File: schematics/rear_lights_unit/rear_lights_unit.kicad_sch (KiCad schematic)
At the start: 0 parts

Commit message: schematic updates for bike computer, rear light unit, rear light unit control box
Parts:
- added BT1: Battery_Cell, symbol Device:Battery_Cell
- added C1, C3: 10nF, symbol Device:C
- added C2, C4: 10uF, symbol Device:C
- added D1, D10, D11, D12, D13, D14, D15, D16, D17, D18, D19, D2, D20, D21, D22, D23, D24, D3, D4, D5, D6, D7, D8, D9: LED, symbol Device:LED
- added J1: Conn_01x04_Socket, symbol Connector:Conn_01x04_Socket
- added Q1, Q2: IRLZ44N, Package_TO_SOT_THT:TO-220-3_Vertical, symbol Transistor_FET:IRLZ44N
- added R1, R10, R11, R12, R13, R14, R15, R16, R17, R18, R19, R2, R20, R21, R22, R23, R24, R3, R4, R5, R6, R7, R8, R9: 120, symbol Device:R
- added R25, R29: 7.5k, symbol Device:R
- added R26, R30: 75k, symbol Device:R
- added R27, R32: 100, symbol Device:R
- added R28, R31: 10k, symbol Device:R
- added U1, U2: LMC555xN, Package_DIP:DIP-8_W7.62mm, symbol Timer:LMC555xN
- added U3: TP4056 module, ..., symbol FarrhadTech:TP4056
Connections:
- new net: D1.1 (K), D2.1 (K), D3.1 (K), D4.1 (K), D5.1 (K), D6.1 (K), D7.1 (K), D8.1 (K), Q1.2 (D)
- new net: D4.2 (A), R4.1
- new net: D7.2 (A), R7.1
- new net: D12.2 (A), R12.1
- new net: D16.2 (A), R16.1
- new net: D10.1 (K), D11.1 (K), D12.1 (K), D13.1 (K), D14.1 (K), D15.1 (K), D16.1 (K), D9.1 (K), Q2.2 (D)
- new net: D11.2 (A), R11.1
- new net: D20.2 (A), R20.1
- new net: D21.2 (A), R21.1
- new net: D1.2 (A), R1.1
- new net: R27.1, U1.3 (Q)
- new net: Q1.1 (G), R27.2, R28.2
- new net: BT1.1 (+), U3.3 (B+)
- new net: BT1.2 (-), U3.4 (B-)
- new net: C4.2, R30.1, U2.2 (TR), U2.6 (THR)
- new net: R29.1, R30.2, U2.7 (DIS)
- new net: D23.2 (A), R23.1
- new net: D8.2 (A), R8.1
- new net: D18.2 (A), R18.1
- new net: D6.2 (A), R6.1
- new net: D5.2 (A), R5.1
- new net: D24.2 (A), R24.1
- new net: D14.2 (A), R14.1
- new net: D10.2 (A), R10.1
- new net: Q2.1 (G), R31.2, R32.2
- new net: D9.2 (A), R9.1
- new net: R25.1, R26.2, U1.7 (DIS)
- new net: C2.2, R26.1, U1.2 (TR), U1.6 (THR)
- new net: D3.2 (A), R3.1
- new net: D2.2 (A), R2.1
- new net: D15.2 (A), R15.1
- new net: C1.1, U1.5 (CV)
- new net: D13.2 (A), R13.1
- new net: D19.2 (A), R19.1
- new net: R32.1, U2.3 (Q)
- new net: D22.2 (A), R22.1
- new net: D17.2 (A), R17.1
- new net: C3.1, U2.5 (CV)
- new net GND: C1.2, C2.1, C3.2, C4.1, D17.1 (K), D18.1 (K), D19.1 (K), D20.1 (K), D21.1 (K), D22.1 (K), D23.1 (K), D24.1 (K), J1.4 (Pin_4), Q1.3 (S), Q2.3 (S), R28.1, R31.1, U1.1 (GND), U2.1 (GND), U3.5 (OUT-)
- new net LEFT_TURN_EN: J1.2 (Pin_2), R25.2, U1.4 (R)
- new net RIGHT_TURN_EN: J1.1 (Pin_1), R29.2, U2.4 (R)
- new net V+: J1.3 (Pin_3), R1.2, R10.2, R11.2, R12.2, R13.2, R14.2, R15.2, R16.2, R17.2, R18.2, R19.2, R2.2, R20.2, R21.2, R22.2, R23.2, R24.2, R3.2, R4.2, R5.2, R6.2, R7.2, R8.2, R9.2, U1.8 (VCC), U2.8 (VCC), U3.5 (OUT-)
- no-connect marks 0 -> 2
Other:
- note added: "D"
- note added: "G"
- note added: "JST connector (right angle)"
- note added: "LEFT TURN SIGNAL: yellow LEDs, flash when on"
- note added: "NOTES All LEDs used are CHANZON brand, 5 mm packages. Each has a forward voltage of 2 V and a forward current of 20 mA. To calculate the current limiting resistor value at maximum battery voltage: V = IR ->(4.2 V - 2 V) = (20 mA)R -> R = 110 ohms To allow for resistor tolerances, I rounded up to the next standard value of 120 ohms. To calculate the current through the LEDs at minimum battery volt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"
- note added: "REAR LIGHT: red LEDs, always on"
- note added: "RIGHT TURN SIGNAL: yellow LEDs, flash when on"
- note added: "S"
- note added: "Samsung 30Q 18650 (3000 mAH, 3.7 V nominal)"

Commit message: more schematic updates
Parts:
- added SW1: rocker_switch, symbol Switch:SW_SPST
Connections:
- net V+: now also SW1.2 (B); no longer U3.5 (OUT-)
- new net: SW1.1 (A), U3.5 (OUT-)
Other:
- note added: "NOTES All LEDs used are CHANZON brand, 5 mm packages. Each has a forward voltage of 2 V and a forward current of 20 mA. To calculate the current limiting resistor value at maximum battery voltage: V = IR =(4.2 V - 2 V) = (20 mA)R -> R = 110 ohms. To account for resistor tolerances, I rounded up to the next standard value of 120 ohms. Calculating the current through the LEDs at minimum battery vol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"
- note added: "This switch connects the rest of the system to the battery for power. Make sure it is turned to the "off" position when charging the battery to ensure correct operation!"
- note added: "right angle JST"
- note removed: "JST connector (right angle)"
- note removed: "NOTES All LEDs used are CHANZON brand, 5 mm packages. Each has a forward voltage of 2 V and a forward current of 20 mA. To calculate the current limiting resistor value at maximum battery voltage: V = IR ->(4.2 V - 2 V) = (20 mA)R -> R = 110 ohms To allow for resistor tolerances, I rounded up to the next standard value of 120 ohms. To calculate the current through the LEDs at minimum battery volt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"
- moved on the sheet: BT1, C1, C2, C3, C4, D1, D10, D11, D12, D13, D14, D15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

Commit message: finalized rear light unit schematic, added corresponding BOM
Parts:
- removed SW1: rocker_switch, symbol Switch:SW_SPST
- added C5: 10uF, symbol Device:C
- added SW2: rocker_switch, symbol Switch:SW_SPST
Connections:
- net GND: now also C5.2
- net V+: now also C5.1, SW2.2 (B)
- new net: SW2.1 (A), U3.5 (OUT-)
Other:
- note added: "This connector breaks out the signals to/from the control box (on handlebars)"

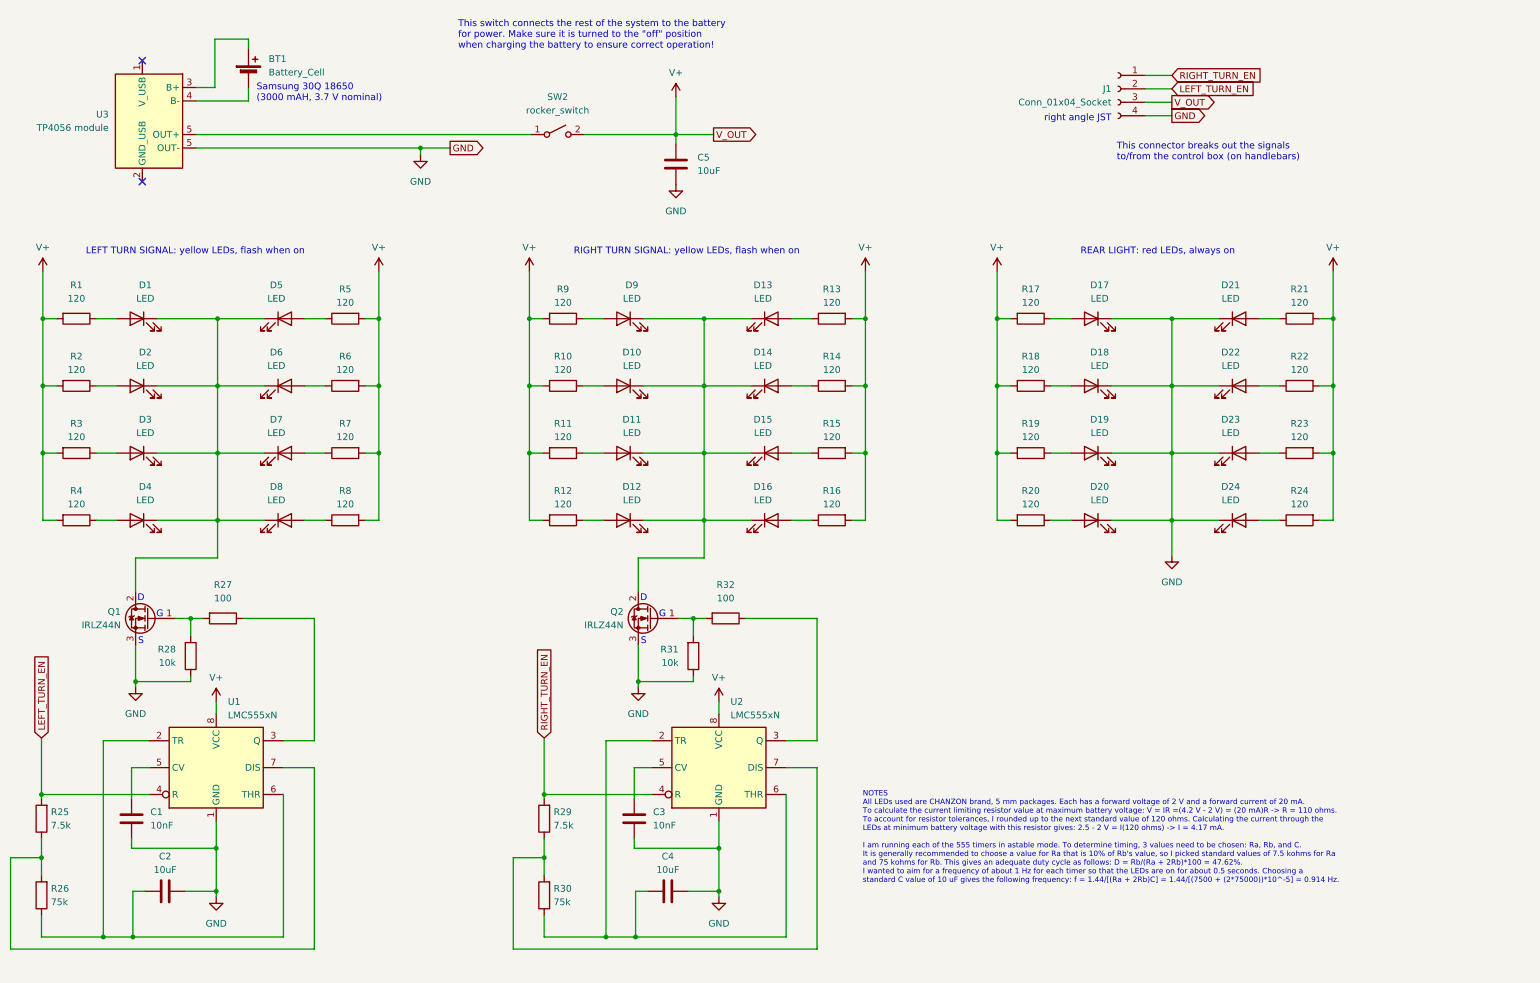
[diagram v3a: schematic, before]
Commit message: rear light unit: finished first draft of PCB, regenerated all related files
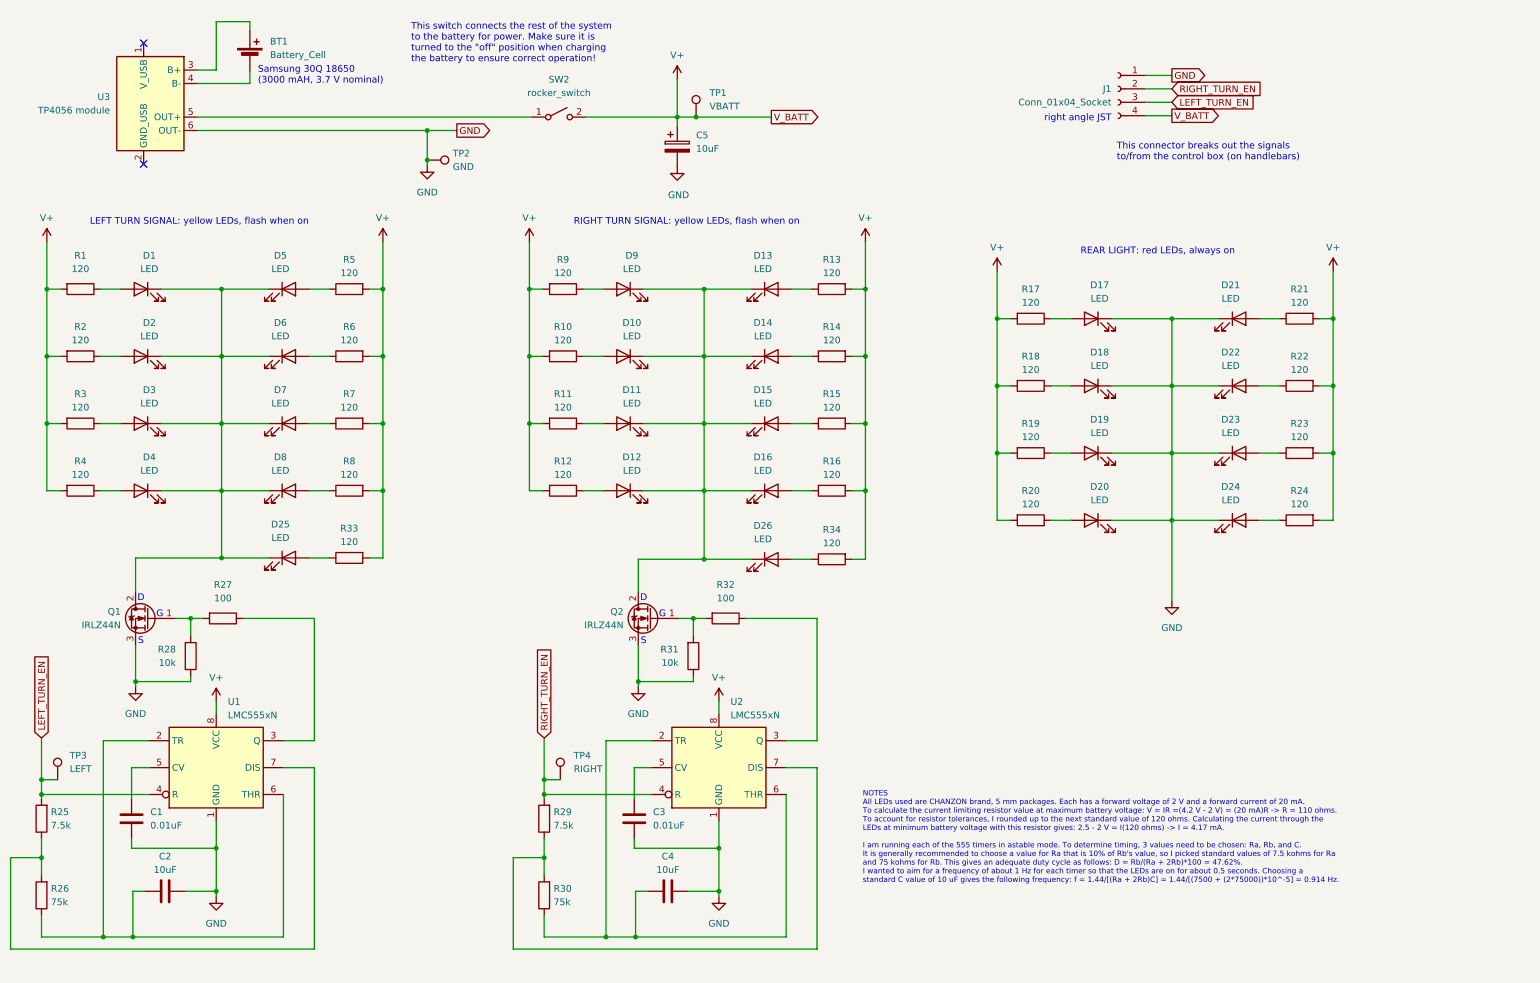
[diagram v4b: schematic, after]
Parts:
- removed C5: 10uF, symbol Device:C
- added C5: 10uF, Capacitor_THT:CP_Radial_D5.0mm_P2.00mm, symbol Device:C_Polarized
- added D25, D26: LED, LED_THT:LED_D5.0mm, symbol Device:LED
- added R33, R34: 120, Resistor_THT:R_Axial_DIN0207_L6.3mm_D2.5mm_P10.16mm_Horizontal, symbol Device:R
- added TP1: VBATT, TestPoint:TestPoint_Keystone_5000-5004_Miniature, symbol Connector:TestPoint
- added TP2: GND, TestPoint:TestPoint_Keystone_5000-5004_Miniature, symbol Connector:TestPoint
- added TP3: LEFT, TestPoint:TestPoint_Keystone_5000-5004_Miniature, symbol Connector:TestPoint
- added TP4: RIGHT, TestPoint:TestPoint_Keystone_5000-5004_Miniature, symbol Connector:TestPoint
- BT1: footprint (none) -> FarrhadTech:BatteryHolder_18650; Part Num (none) -> Samsung 30Q 18650
- C1, C3: value 10nF -> 0.01uF; footprint (none) -> Capacitor_THT:C_Rect_L4.6mm_W2.0mm_P2.50mm_MKS02_FKP02; Part Num (none) -> K103K15X7RF5TK2
- C2, C4: footprint (none) -> Capacitor_THT:C_Rect_L4.6mm_W2.0mm_P2.50mm_MKS02_FKP02; Part Num (none) -> FG18X5R1E106MRT06
- D1, D10, D11, D12, D13, D14, D15, D16, D17, D18, D19, D2, D20, D21, D22, D23, D24, D3, D4, D5, D6, D7, D8, D9: footprint (none) -> LED_THT:LED_D5.0mm; Part Num (none) -> Chanzon LED
- J1: footprint (none) -> Connector_JST:JST_XH_S4B-XH-A_1x04_P2.50mm_Horizontal; Part Num (none) -> JST XH-2.54
- Q1, Q2: footprint Package_TO_SOT_THT:TO-220-3_Vertical -> FarrhadTech:TO-220-3_Horizontal_TabUpNoHole; Part Num (none) -> IRLZ44N
- R1, R10, R11, R12, R13, R14, R15, R16, R17, R18, R19, R2, R20, R21, R22, R23, R24, R3, R4, R5, R6, R7, R8, R9: footprint (none) -> Resistor_THT:R_Axial_DIN0207_L6.3mm_D2.5mm_P10.16mm_Horizontal; Part Num (none) -> MFR-25SFTF52-120R
- R25, R29: footprint (none) -> Resistor_THT:R_Axial_DIN0207_L6.3mm_D2.5mm_P10.16mm_Horizontal; Part Num (none) -> MFR-25FTE52-7K5
- R26, R30: footprint (none) -> Resistor_THT:R_Axial_DIN0207_L6.3mm_D2.5mm_P10.16mm_Horizontal; Part Num (none) -> MFR-25FTE52-75K
- R27, R32: footprint (none) -> Resistor_THT:R_Axial_DIN0207_L6.3mm_D2.5mm_P10.16mm_Horizontal; Part Num (none) -> MFR-25SFTF52-100R
- R28, R31: footprint (none) -> Resistor_THT:R_Axial_DIN0207_L6.3mm_D2.5mm_P10.16mm_Horizontal; Part Num (none) -> MFR-25SFRF52-10K
- SW2: footprint (none) -> Button_Switch_THT:SW_Lever_1P2T_NKK_GW12LxH; Part Num (none) -> GW12LCH
- U1, U2: Part Num (none) -> LMC555CN/NOPB
- U3: footprint ... -> FarrhadTech:TP4065; Part Num (none) -> TP4056 module
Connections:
- net GND: now also J1.1 (Pin_1), U3.6 (OUT-), C5.2, TP2.1; no longer J1.4 (Pin_4), U3.5 (OUT-)
- net LEFT_TURN_EN: now also J1.3 (Pin_3), TP3.1; no longer J1.2 (Pin_2)
- net RIGHT_TURN_EN: now also J1.2 (Pin_2), TP4.1; no longer J1.1 (Pin_1)
- net V+: now also J1.4 (Pin_4), C5.1, R33.2, R34.2, TP1.1; no longer J1.3 (Pin_3)
- net at D1.1 (K), D2.1 (K), D3.1 (K)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: now also D25.1 (K)
- net at D10.1 (K), D11.1 (K), D12.1 (K)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: now also D26.1 (K)
- new net: D26.2 (A), R34.1
- new net: D25.2 (A), R33.1
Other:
- moved on the sheet: BT1, D1, D10, D11, D12, D13, D14, D15, D16, D2, D3, D4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

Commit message: finalized rear light unit v0
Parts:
- removed SW2: rocker_switch, Button_Switch_THT:SW_Lever_1P2T_NKK_GW12LxH, symbol Switch:SW_SPST
- added SW1: GW12LxH, FarrhadTech:SW_Lever_1P2T_NKK_GW12LxH, symbol FarrhadTech:GW12LxH
- U3: footprint FarrhadTech:TP4065 -> FarrhadTech:TP4056_module
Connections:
- net V+: now also SW1.4
- net at U3.5 (OUT+): now also SW1.5
- no-connect marks 2 -> 3
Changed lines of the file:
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@@
 		(at 41.91 43.18)
 	)
+	(no_connect
+		(at 125.476 31.75)
+	)
 	(wire
 		(pts
@@
 	(wire
 		(pts
+			(xy 127.254 36.83) (xy 127.254 34.29)
+		)
+		(stroke
+			(width 0)
+			(type default)
+		)
+	)
+	(wire
+		(pts
 			(xy 163.322 152.146) (xy 169.164 152.146)
 		)
@@
 	(wire
 		(pts
+			(xy 127.254 34.29) (xy 142.748 34.29)
+		)
+		(stroke
+			(width 0)
+			(type default)
+		)
+	)
+	(wire
+		(pts
 			(xy 213.36 85.09) (xy 217.17 85.09)
 		)
@@
 	(wire
 		(pts
-			(xy 125.476 34.29) (xy 142.748 34.29)
-		)
-		(stroke
-			(width 0)
-			(type default)
-		)
-	)
-	(wire
-		(pts
 			(xy 45.212 104.902) (xy 56.642 104.902)
 		)
@@
 	(wire
 		(pts
+			(xy 125.476 36.83) (xy 127.254 36.83)
+		)
+		(stroke
+			(width 0)
+			(type default)
+		)
+	)
+	(wire
+		(pts
 			(xy 169.164 157.226) (xy 169.164 191.516)
 		)
@@
 	(text "This switch connects the rest of the system \nto the battery for power. Make sure it is \nturned to the \"off\" position when charging \nthe battery to ensure correct operation!"
 		(exclude_from_sim no)
-		(at 92.456 20.32 0)
+		(at 94.996 18.796 0)
 		(effects
 			(font
@@
 			)
 		)
-		(property "Footprint" "FarrhadTech:TP4065"
+		(property "Footprint" "FarrhadTech:TP4056_module"
 			(at 39.37 48.26 0)
 			(effects
@@
 	)
 	(symbol
-		(lib_id "Switch:SW_SPST")
-		(at 120.396 34.29 0)
-		(unit 1)
-		(exclude_from_sim no)
-		(in_bom yes)
-		(on_board yes)
-		(dnp no)
-		(fields_autoplaced yes)
-		(property "Reference" "SW2"
-			(at 120.396 27.178 0)
-			(effects
-				(font
-					(size 1.27 1.27)
-				)
-			)
-		)
-		(property "Value" "rocker_switch"
-			(at 120.396 29.718 0)
-			(effects
-				(font
-					(size 1.27 1.27)
-				)
-			)
-		)
-		(property "Footprint" "Button_Switch_THT:SW_Lever_1P2T_NKK_GW12LxH"
-			(at 120.396 34.29 0)
-			(effects
-				(font
-					(size 1.27 1.27)
-				)
-				(hide yes)
-			)
-		)
-		(property "Datasheet" "~"
-			(at 120.396 34.29 0)
-			(effects
-				(font
-					(size 1.27 1.27)
-				)
-				(hide yes)
-			)
-		)
-		(property "Description" "SPDT rocker switch, red"
-			(at 120.396 34.29 0)
-			(effects
-				(font
-					(size 1.27 1.27)
-				)
-				(hide yes)
-			)
-		)
-		(property "Part Num" "GW12LCH"
-			(at 120.396 34.29 0)
-			(effects
-				(font
-					(size 1.27 1.27)
-				)
-				(hide yes)
-			)
-		)
-		(pin "1"
-		)
-		(pin "2"
-		)
-		(instances
-			(project "rear_lights_unit"
-				(path "/d7503315-c43d-483b-8e44-2a129b61c505"
-					(reference "SW2")
-					(unit 1)
-				)
-			)
-		)
-	)
-	(symbol
 		(lib_id "Device:LED")
 		(at 160.528 92.202 0)
@@
 					(unit 1)
 				)
+			)
+		)
+	)
+	(symbol
+		(lib_id "FarrhadTech:GW12LxH")
+		(at 120.396 34.29 0)
+		(unit 1)
+		(exclude_from_sim no)
+		(in_bom yes)
+		(on_board yes)
+		(dnp no)
+		(fields_autoplaced yes)
+		(property "Reference" "SW1"
+			(at 120.396 25.4 0)
+			(effects
+				(font
+					(size 1.27 1.27)
+				)
+			)
+		)
+		(property "Value" "GW12LxH"
+			(at 120.396 27.94 0)
+			(effects
+				(font
+					(size 1.27 1.27)
+				)
+			)
+		)
+		(property "Footprint" "FarrhadTech:SW_Lever_1P2T_NKK_GW12LxH"
+			(at 120.396 34.29 0)
+			(effects
+				(font
+					(size 1.27 1.27)
+				)
+				(hide yes)
+			)
+		)
+		(property "Datasheet" "~"
+			(at 120.396 41.91 0)
+			(effects
+				(font
+					(size 1.27 1.27)
+				)
+				(hide yes)
+			)
+		)
+		(property "Description" "SPDT paddle switch, red, right-angle"
+			(at 120.396 34.29 0)
+			(effects
+				(font
+					(size 1.27 1.27)
+				)
+				(hide yes)
+			)
+		)
+		(property "Part Num" "GW12LCH"
+			(at 120.396 34.29 0)
+			(effects
+				(font
+					(size 1.27 1.27)
+				)
+				(hide yes)
+			)
+		)
+		(pin "4"
+		)
+		(pin "5"
+		)
+		(pin "6"
+		)
+		(instances
+			(project ""
+				(path "/d7503315-c43d-483b-8e44-2a129b61c505"
+					(reference "SW1")
+					(unit 1)
+				)

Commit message: updated both sets of light unit board files to include the newly-added 3D models
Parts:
- BT1: footprint FarrhadTech:BatteryHolder_18650 -> FahrradTech:BatteryHolder_18650
- Q1, Q2: footprint FarrhadTech:TO-220-3_Horizontal_TabUpNoHole -> FahrradTech:TO-220-3_Horizontal_TabUpNoHole
- SW1: footprint FarrhadTech:SW_Lever_1P2T_NKK_GW12LxH -> FahrradTech:SW_Lever_1P2T_NKK_GW12LxH
- TP1, TP2, TP3, TP4: footprint TestPoint:TestPoint_Keystone_5000-5004_Miniature -> FahrradTech:TestPoint_Keystone_5000-5004_Miniature
- U3: footprint FarrhadTech:TP4056_module -> FahrradTech:TP4056_module
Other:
- title: FarrhadTech Rear Lights Unit -> FahrradTech Rear Lights Unit
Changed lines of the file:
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@@
 	(paper "A4")
 	(title_block
-		(title "FarrhadTech Rear Lights Unit")
+		(title "FahrradTech Rear Lights Unit")
 		(date "2025-03-28")
 		(rev "0")
@@
 			)
 		)
-		(property "Footprint" "TestPoint:TestPoint_Keystone_5000-5004_Miniature"
+		(property "Footprint" "FahrradTech:TestPoint_Keystone_5000-5004_Miniature"
 			(at 30.734 159.512 0)
 			(effects
@@
 			)
 		)
-		(property "Footprint" "FarrhadTech:TO-220-3_Horizontal_TabUpNoHole"
+		(property "Footprint" "FahrradTech:TO-220-3_Horizontal_TabUpNoHole"
 			(at 37.846 130.937 0)
 			(effects
@@
 			)
 		)
-		(property "Footprint" "FarrhadTech:TP4056_module"
+		(property "Footprint" "FahrradTech:TP4056_module"
 			(at 39.37 48.26 0)
 			(effects
@@
 			)
 		)
-		(property "Footprint" "TestPoint:TestPoint_Keystone_5000-5004_Miniature"
+		(property "Footprint" "FahrradTech:TestPoint_Keystone_5000-5004_Miniature"
 			(at 151.384 34.29 0)
 			(effects
@@
 			)
 		)
-		(property "Footprint" "TestPoint:TestPoint_Keystone_5000-5004_Miniature"
+		(property "Footprint" "FahrradTech:TestPoint_Keystone_5000-5004_Miniature"
 			(at 95.504 47.498 0)
 			(effects
@@
 			)
 		)
-		(property "Footprint" "TestPoint:TestPoint_Keystone_5000-5004_Miniature"
+		(property "Footprint" "FahrradTech:TestPoint_Keystone_5000-5004_Miniature"
 			(at 125.73 159.512 0)
 			(effects
@@
 			)
 		)
-		(property "Footprint" "FarrhadTech:BatteryHolder_18650"
+		(property "Footprint" "FahrradTech:BatteryHolder_18650"
 			(at 61.976 21.59 90)
 			(effects
@@
 			)
 		)
-		(property "Footprint" "FarrhadTech:TO-220-3_Horizontal_TabUpNoHole"
+		(property "Footprint" "FahrradTech:TO-220-3_Horizontal_TabUpNoHole"
 			(at 132.842 130.937 0)
 			(effects
@@
 			)
 		)
-		(property "Footprint" "FarrhadTech:SW_Lever_1P2T_NKK_GW12LxH"
+		(property "Footprint" "FahrradTech:SW_Lever_1P2T_NKK_GW12LxH"
 			(at 120.396 34.29 0)
 			(effects
